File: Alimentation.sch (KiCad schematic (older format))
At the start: 21 parts, among them P1 Prise_Equilibrage, P10 CONN_01X02, P2 Prise_Alim, P3 Prise_Batterie, P4 ConnecteurBippeur, P5 CONN_01X04, P6 CAN_conn, P7 CAN_conn, P8 CONN_01X02, P9 CONN_01X02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

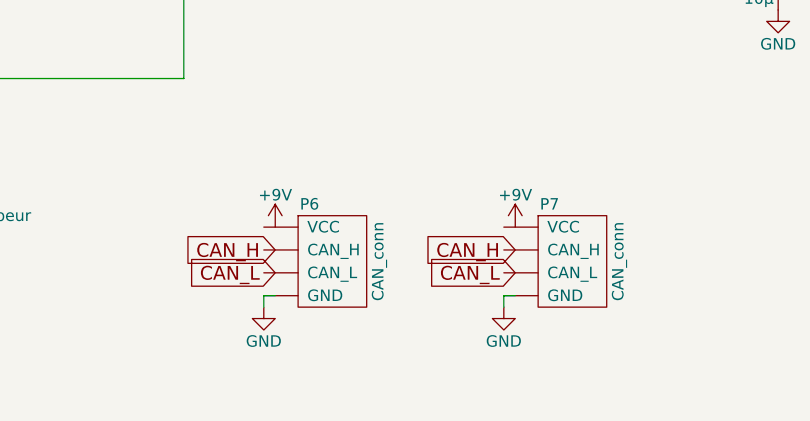
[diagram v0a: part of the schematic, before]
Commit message: retourné connecteur CAN
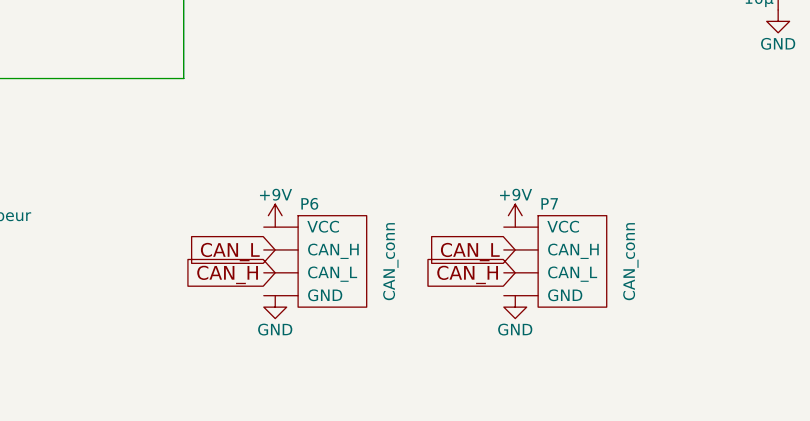
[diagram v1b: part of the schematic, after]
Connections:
- wire segments 30 -> 26
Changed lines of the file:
@@
 L GND #PWR05
 U 1 1 58854155
-P 4750 4700
-F 0 "#PWR05" H 4750 4450 50  0001 C CNN
-F 1 "GND" H 4750 4550 50  0000 C CNN
-F 2 "" H 4750 4700 50  0000 C CNN
-F 3 "" H 4750 4700 50  0000 C CNN
-	1    4750 4700
+P 4800 4650
+F 0 "#PWR05" H 4800 4400 50  0001 C CNN
+F 1 "GND" H 4800 4500 50  0000 C CNN
+F 2 "" H 4800 4650 50  0000 C CNN
+F 3 "" H 4800 4650 50  0000 C CNN
+	1    4800 4650
 	1    0    0    -1
 $EndComp
@@
 L GND #PWR09
 U 1 1 5892954C
-P 3700 4700
-F 0 "#PWR09" H 3700 4450 50  0001 C CNN
-F 1 "GND" H 3700 4550 50  0000 C CNN
-F 2 "" H 3700 4700 50  0000 C CNN
-F 3 "" H 3700 4700 50  0000 C CNN
-	1    3700 4700
-	1    0    0    -1
-$EndComp
-Wire Wire Line
-	3750 4650 3700 4650
-Wire Wire Line
-	3700 4650 3700 4700
-Wire Wire Line
-	4800 4650 4750 4650
-Wire Wire Line
-	4750 4650 4750 4700
+P 3750 4650
+F 0 "#PWR09" H 3750 4400 50  0001 C CNN
+F 1 "GND" H 3750 4500 50  0000 C CNN
+F 2 "" H 3750 4650 50  0000 C CNN
+F 3 "" H 3750 4650 50  0000 C CNN
+	1    3750 4650
+	1    0    0    -1
+$EndComp
 $Comp
 L +9V #PWR010
@@
 	1    0    0    -1
 $EndComp
+Text GLabel 4800 4550 0    60   Input ~ 0
+CAN_H
 Text GLabel 4800 4450 0    60   Input ~ 0
+CAN_L
+Text GLabel 3750 4550 0    60   Input ~ 0
 CAN_H
-Text GLabel 4800 4550 0    60   Input ~ 0
-CAN_L
 Text GLabel 3750 4450 0    60   Input ~ 0
-CAN_H
-Text GLabel 3750 4550 0    60   Input ~ 0
 CAN_L
 $Comp
@@
 P 4950 4500
 F 0 "P7" H 4950 4750 50  0000 C CNN
-F 1 "CAN_conn" V 5250 4500 50  0000 C CNN
+F 1 "CAN_conn" V 5300 4500 50  0000 C CNN
 F 2 "Connectors_JST:JST_XH_B04B-XH-A_04x2.50mm_Straight" H 4950 4500 50  0001 C CNN
 F 3 "" H 4950 4500 50  0000 C CNN
@@
 P 3900 4500
 F 0 "P6" H 3900 4750 50  0000 C CNN
-F 1 "CAN_conn" V 4200 4500 50  0000 C CNN
+F 1 "CAN_conn" V 4250 4500 50  0000 C CNN
 F 2 "Connectors_JST:JST_XH_B04B-XH-A_04x2.50mm_Straight" H 3900 4500 50  0001 C CNN
 F 3 "" H 3900 4500 50  0000 C CNN

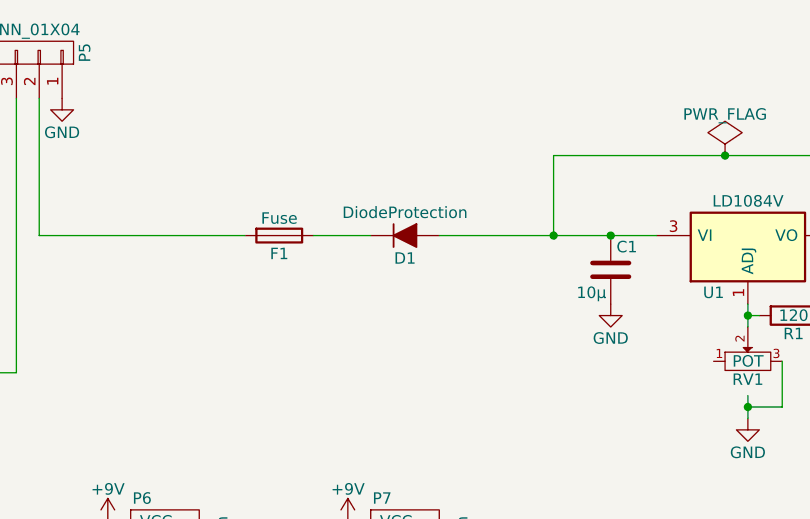
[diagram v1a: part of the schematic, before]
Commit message: corrige sens diode D1
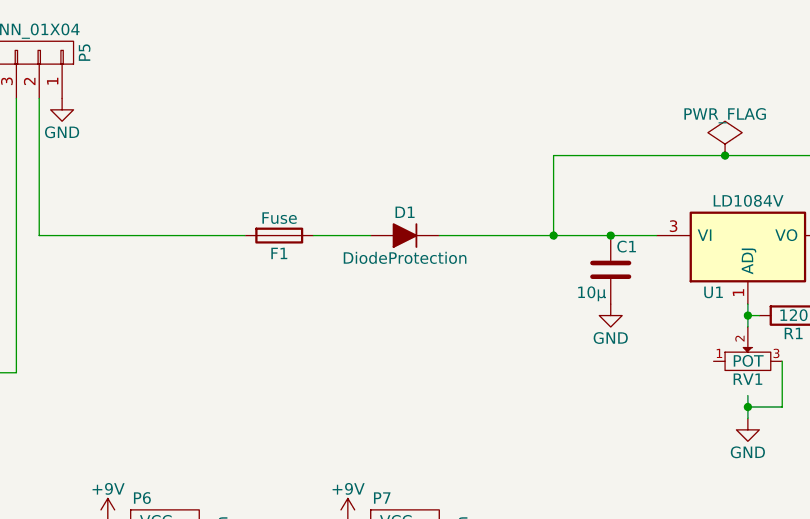
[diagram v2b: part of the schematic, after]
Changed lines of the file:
@@
 LIBS:PhoenixRobotik
 LIBS:STMicroelectronics
+LIBS:Alimentation-cache
 EELAYER 25 0
 EELAYER END
@@
 F 3 "" H 5050 3100 50  0000 C CNN
 	1    5050 3100
-	1    0    0    -1
+	-1   0    0    1
 $EndComp
 Text Notes 1650 4150 0    60   ~ 12
